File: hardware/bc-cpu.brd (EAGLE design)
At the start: 87.6 x 73.7 mm, 88 parts, among them J1 BATTERIES, J2 PHOTO, J3 LED MATRIX, J5 BRK5, U1 R-735.0P, U2 MAX11632EEG+, U3 MAX11632EEG+, U4 AD1584BRTZ

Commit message: Final board, as ordered from OSHPark
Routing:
- net GND: vias 3 -> 7

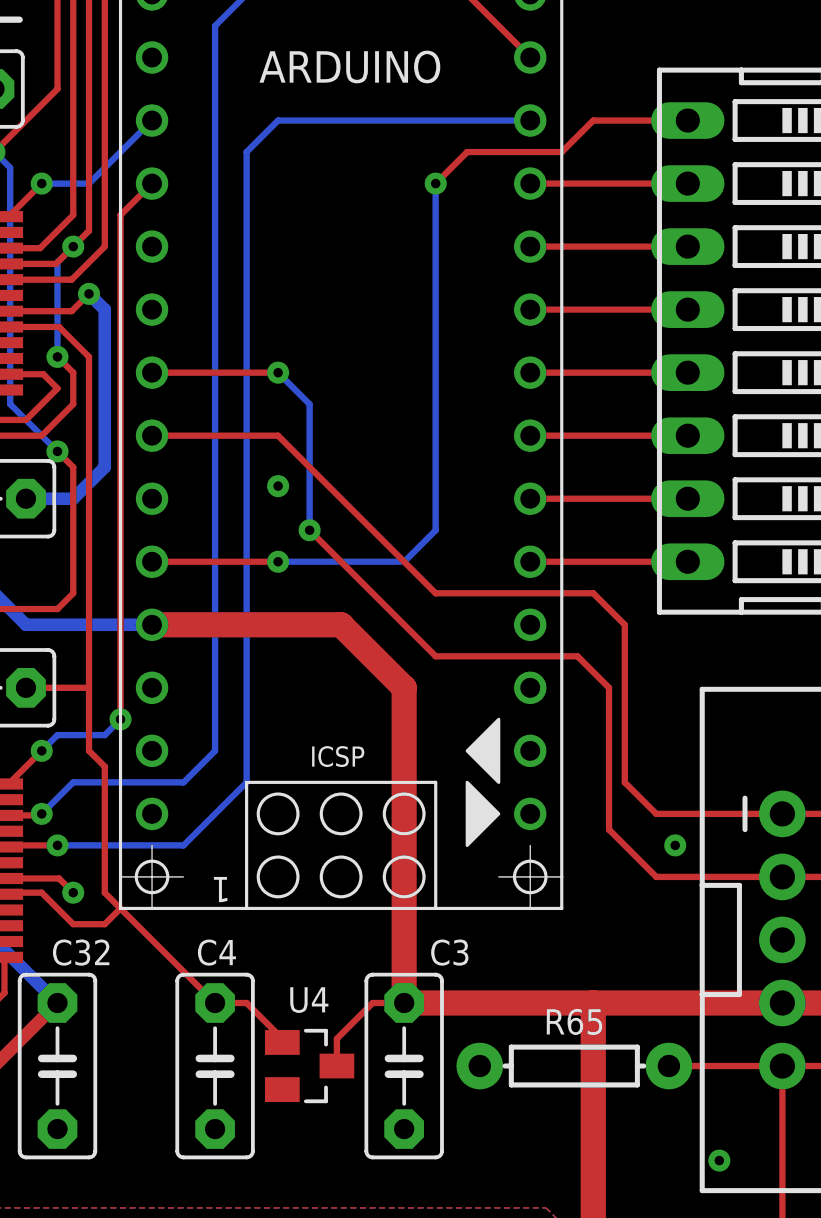
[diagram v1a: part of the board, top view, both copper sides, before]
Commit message: Ambient brightness sensor and reaction
Fixed the hardware -- forgot to wire the photosensor :(

Added display brightness adjustment to the ambient light, with a 10
second averaging.
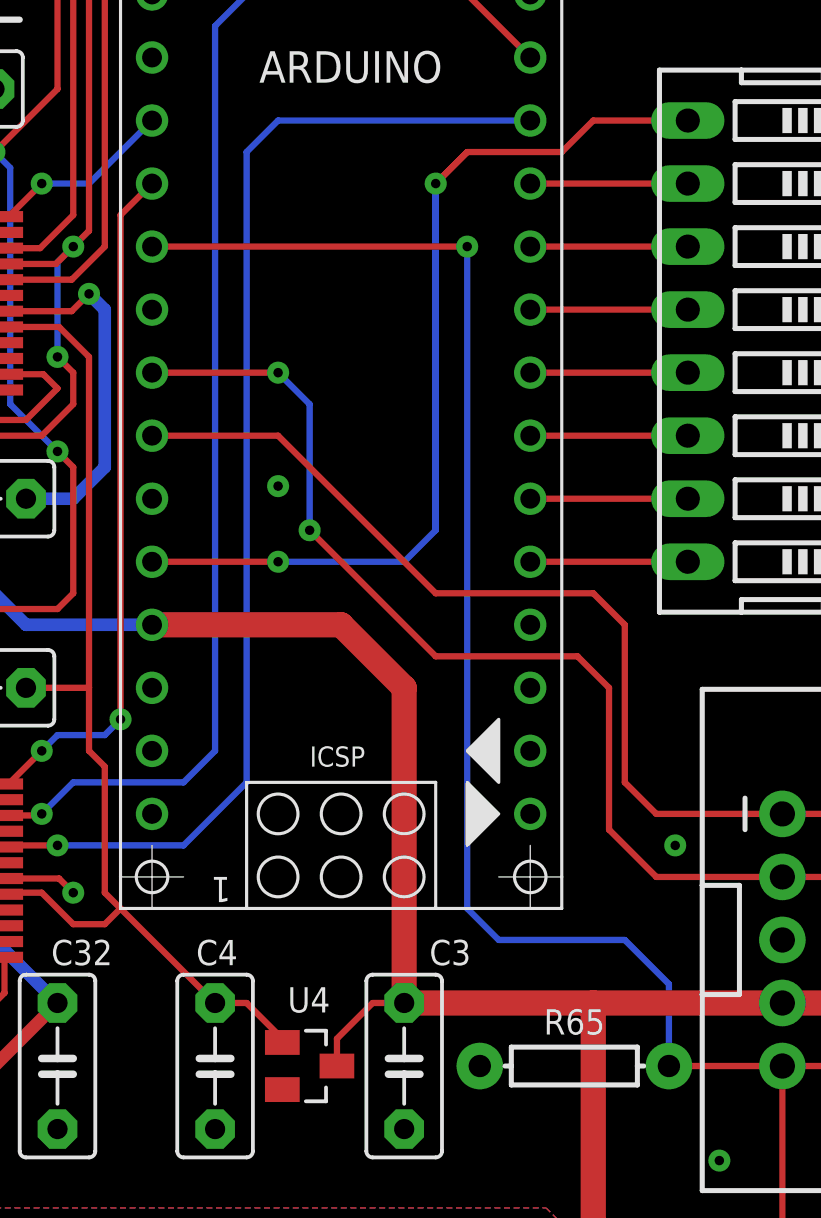
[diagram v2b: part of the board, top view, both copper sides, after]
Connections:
- net PHOTO: now also ARDUINO.6
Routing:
- net PHOTO: track 17.3 -> 69.3 mm, vias 0 -> 1
- net DIP8: track 37.1 -> 80.8 mm
